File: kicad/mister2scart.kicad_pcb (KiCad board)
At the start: 2 copper layers, 49.9 x 43 mm, 11 parts, among them J1 SCART-F, J2 DE15-F, J3 SJ1-3523NG, J4 RCA-F, SW2 SS12D10G6-WJ, U1 MAX662ACPA

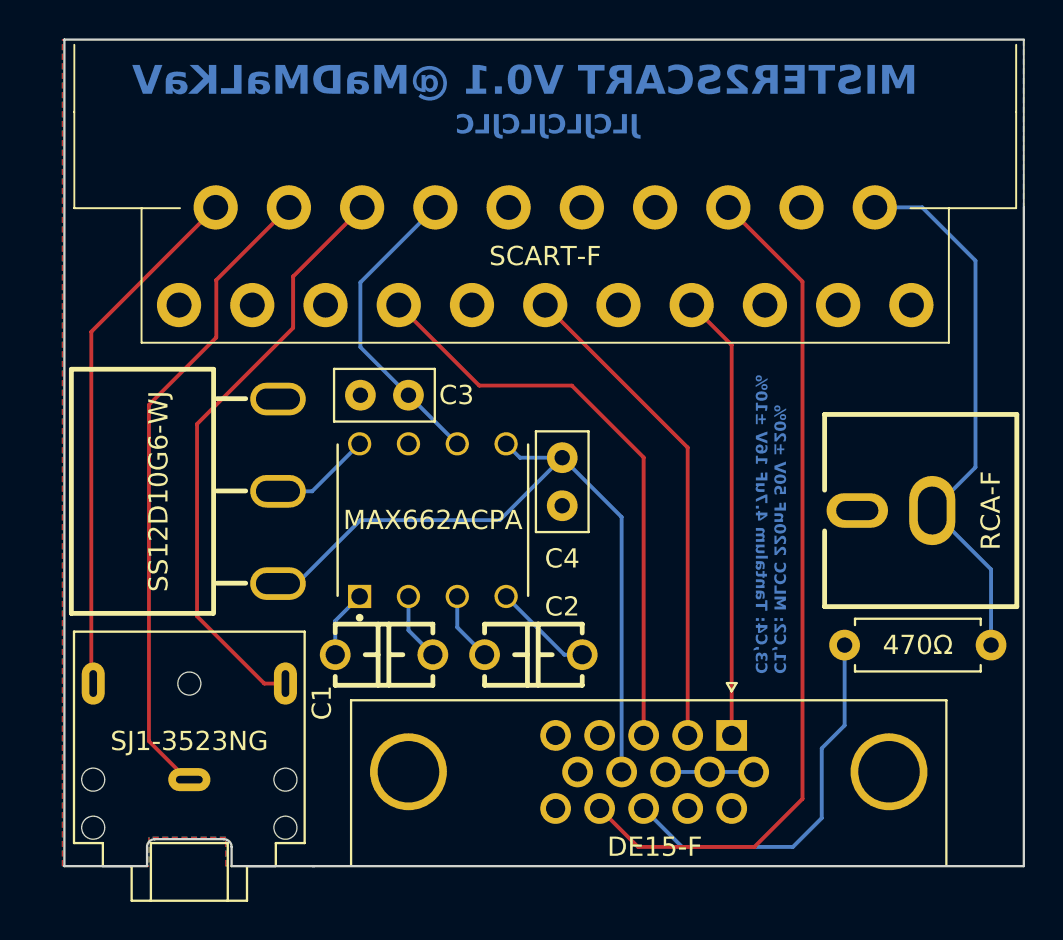
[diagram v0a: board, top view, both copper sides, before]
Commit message: V0.2:
- Corrected pinout of the SCART connection, as SCART to SCART cables have some pins crossed.
- Marked polarity in the silkscreen for polarized capacitors
- Increase footprint for resistor
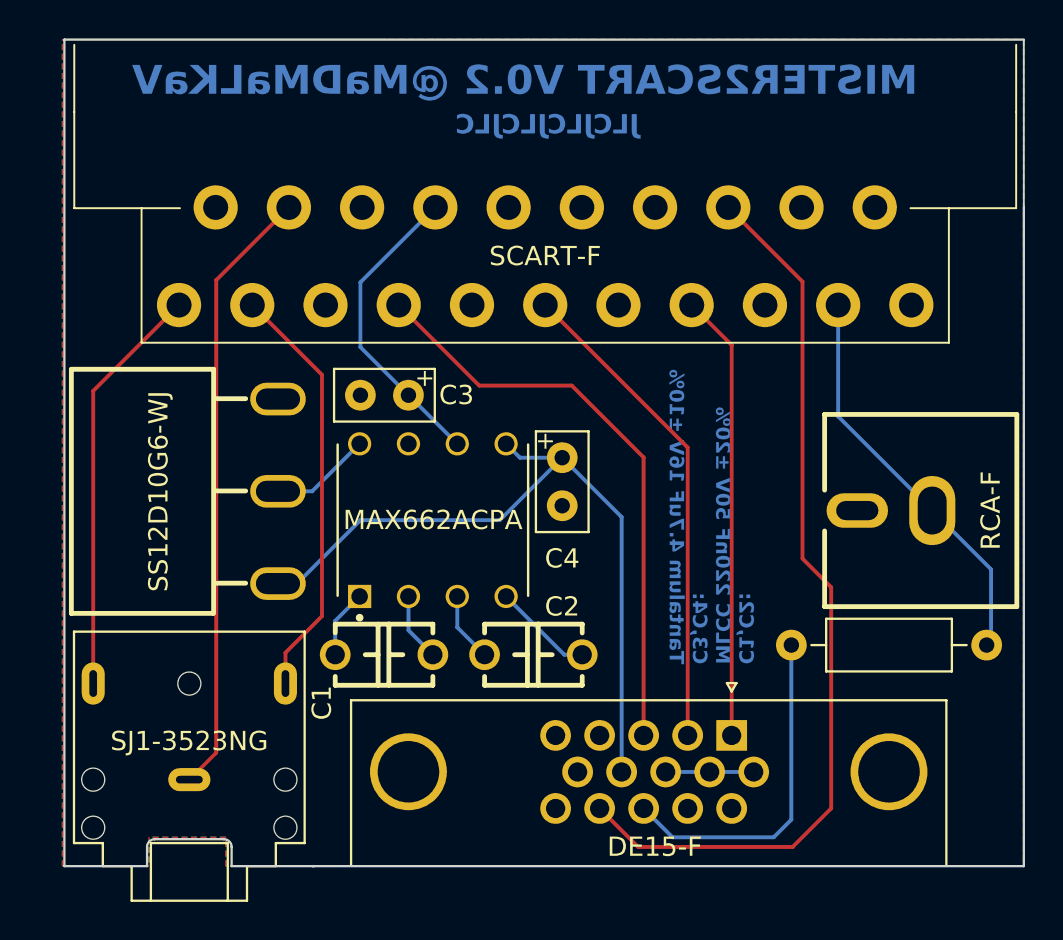
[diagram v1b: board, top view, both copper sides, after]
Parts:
- R1: footprint Resistor_THT:R_Axial_DIN0207_L6.3mm_D2.5mm_P7.62mm_Horizontal -> Resistor_THT:R_Axial_DIN0207_L6.3mm_D2.5mm_P10.16mm_Horizontal
- moved R1 10.4 mm to (141.4, 81.5), turned to 0 degrees
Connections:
- J1 pad 1: unconnected-(J1-P1-Pad1) -> Net-(J1-P1)
- J1 pad 19: unconnected-(J1-P19-Pad19) -> Net-(J1-P19)
- J1 pad 2: Net-(J1-P2) -> unconnected-(J1-P2-Pad2)
- J1 pad 20: Net-(J1-P20) -> unconnected-(J1-P20-Pad20)
- J1 pad 3: unconnected-(J1-P3-Pad3) -> Net-(J1-P3)
- J1 pad 6: Net-(J1-P6) -> unconnected-(J1-P6-Pad6)
- J3 pad R: Net-(J1-P2) -> Net-(J1-P1)
- J3 pad T: Net-(J1-P6) -> Net-(J1-P3)
- J4 pad 1: Net-(J1-P20) -> Net-(J1-P19)
- R1 pad 1: Net-(J1-P20) -> Net-(J2-Pad13)
- R1 pad 2: Net-(J2-Pad13) -> Net-(J1-P19)
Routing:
- net Net-(J1-P6): track 30.8 -> 0.00 mm
- net Net-(J1-P20): track 28.6 -> 0.00 mm
- net Net-(J1-P2): track 27.4 -> 0.00 mm
- net Net-(J1-P3): track 0.00 -> 22.0 mm
- net Net-(J1-P1): track 0.00 -> 21.5 mm
- net Net-(J1-P19): track 0.00 -> 21.0 mm
- net Net-(J2-Pad13): track 20.2 -> 17.8 mm
- net Net-(J1-P16): track 44.8 -> 47.2 mm
- net Net-(J1-P4): track 33.6 -> 31.9 mm
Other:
- board text added: "MISTER2SCART V0.2 @MaDMaLKaV"
- board text removed: "MISTER2SCART V0.1 @MaDMaLKaV"

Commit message: v0.3: fixed sync connector pinout
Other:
- board text added: "MISTER2SCART V0.3 @MaDMaLKaV"
- board text removed: "MISTER2SCART V0.2 @MaDMaLKaV"
